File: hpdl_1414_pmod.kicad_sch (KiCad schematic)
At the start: 2 parts, among them J1 10129382-912001BLF, J2 10129382-912001BLF

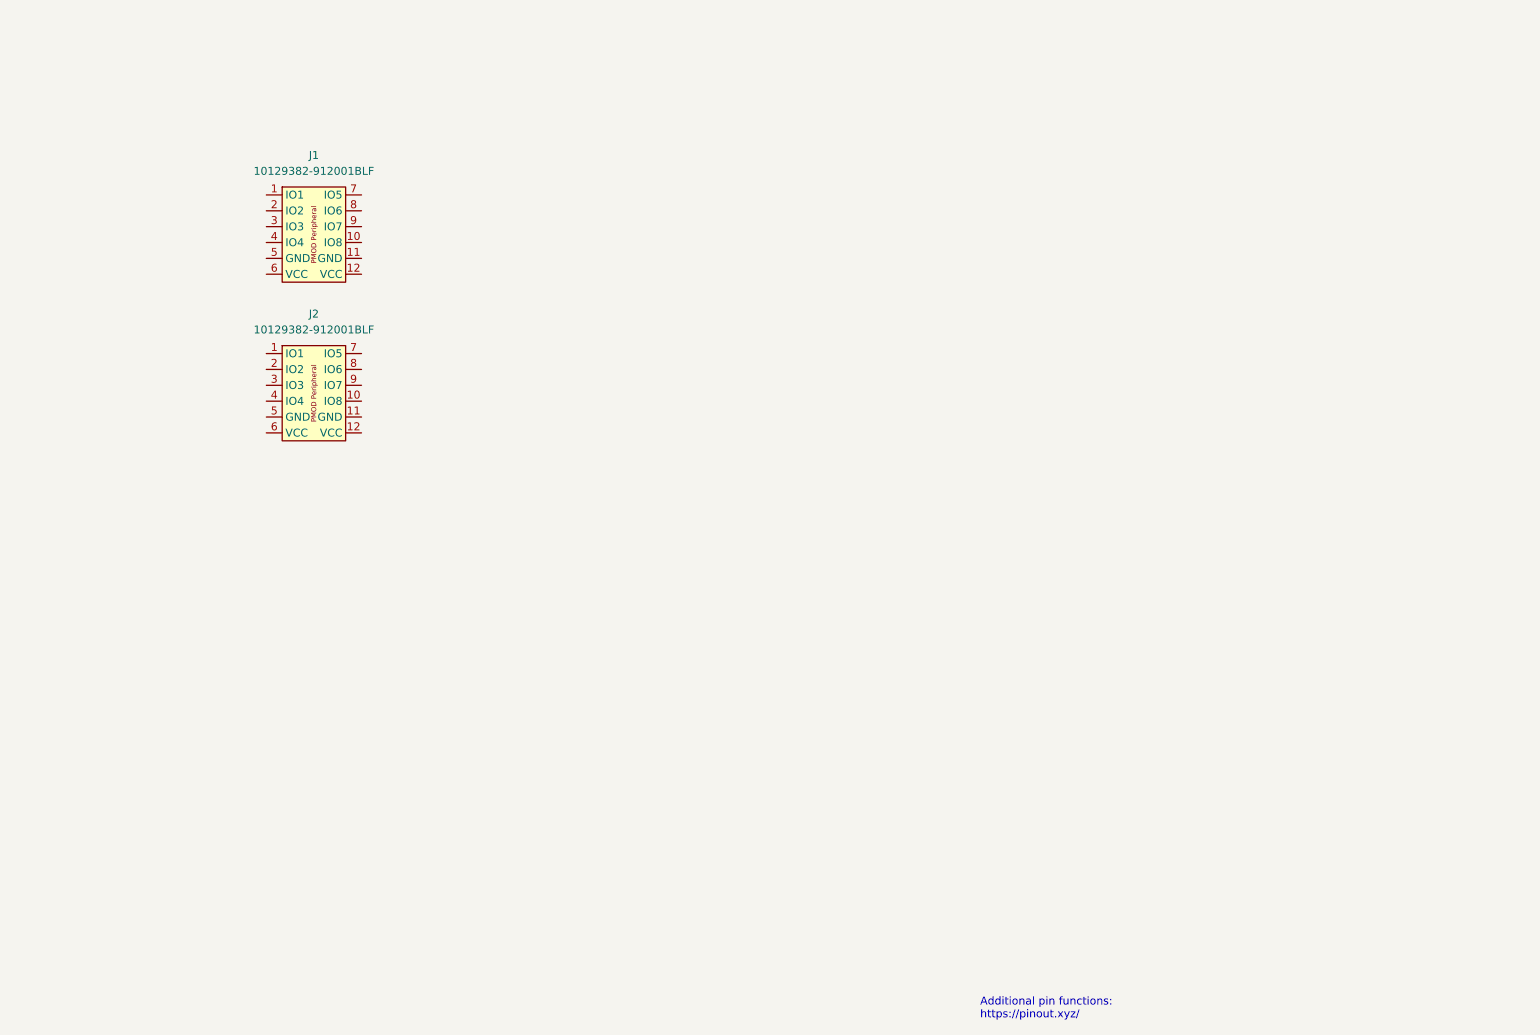
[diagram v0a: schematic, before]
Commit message: Finilize shematic, place components, add 3d models
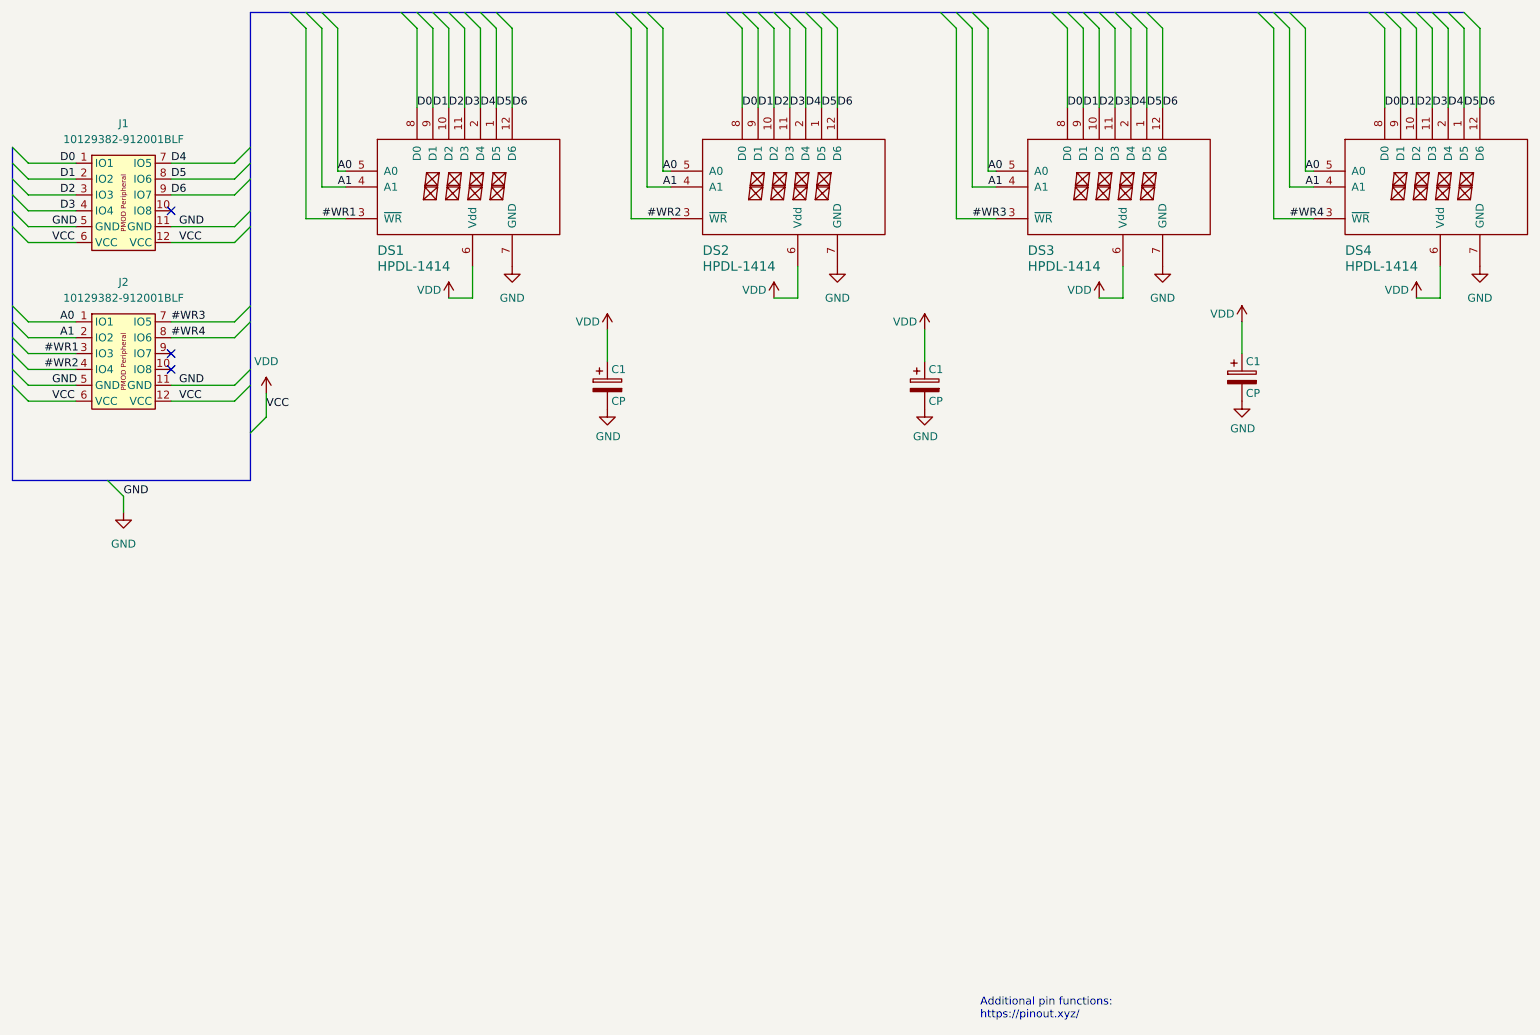
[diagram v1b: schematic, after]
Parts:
- added C1 (x3): CP, Capacitor_THT:C_Disc_D4.3mm_W1.9mm_P5.00mm, symbol Device:CP
- added DS1, DS2, DS3, DS4: HPDL-1414, hpdl_1414:hpdl-1414, symbol hpdl-1414:HPDL-1414
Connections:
- net A0: now reaches J2.1 (IO1)
- net A0: now also DS1.5 (A0), DS2.5 (A0), DS3.5 (A0), DS4.5 (A0)
- net GND: now reaches J2.11 (GND)
- net GND: now also J1.11 (GND), J1.5 (GND), J2.5 (GND), C1.2, C1.2, C1.2, DS1.7 (GND), DS2.7 (GND), DS3.7 (GND), DS4.7 (GND)
- net VDD: now reaches J2.12 (VCC)
- net VDD: now also J1.12 (VCC), J1.6 (VCC), J2.6 (VCC), C1.1, C1.1, C1.1, DS1.6 (Vdd), DS2.6 (Vdd), DS3.6 (Vdd), DS4.6 (Vdd)
- net A1: now reaches J2.2 (IO2)
- net A1: now also DS1.4 (A1), DS2.4 (A1), DS3.4 (A1), DS4.4 (A1)
- net #WR1: now reaches J2.3 (IO3)
- net #WR1: now also DS1.3 (~{WR})
- net #WR2: now reaches J2.4 (IO4)
- net #WR2: now also DS2.3 (~{WR})
- net #WR3: now reaches J2.7 (IO5)
- net #WR3: now also DS3.3 (~{WR})
- net #WR4: now reaches J2.8 (IO6)
- net #WR4: now also DS4.3 (~{WR})
- net D0: now reaches J1.1 (IO1)
- net D0: now also DS1.8 (D0), DS2.8 (D0), DS3.8 (D0), DS4.8 (D0)
- net D1: now reaches J1.2 (IO2)
- net D1: now also DS1.9 (D1), DS2.9 (D1), DS3.9 (D1), DS4.9 (D1)
- net D2: now reaches J1.3 (IO3)
- net D2: now also DS1.10 (D2), DS2.10 (D2), DS3.10 (D2), DS4.10 (D2)
- net D3: now reaches J1.4 (IO4)
- net D3: now also DS1.11 (D3), DS2.11 (D3), DS3.11 (D3), DS4.11 (D3)
- net D4: now reaches J1.7 (IO5)
- net D4: now also DS1.2 (D4), DS2.2 (D4), DS3.2 (D4), DS4.2 (D4)
- net D5: now reaches J1.8 (IO6)
- net D5: now also DS1.1 (D5), DS2.1 (D5), DS3.1 (D5), DS4.1 (D5)
- net D6: now reaches J1.9 (IO7)
- net D6: now also DS1.12 (D6), DS2.12 (D6), DS3.12 (D6), DS4.12 (D6)
- no-connect marks 0 -> 3
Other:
- moved on the sheet: J1, J2

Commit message: Grenerate gerbers, V1.0
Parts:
- added C7: 15uF, Capacitor_SMD:C_1210_3225Metric_Pad1.33x2.70mm_HandSolder, symbol Device:C_Small
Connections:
- net GND: now also C7.1
- net VDD: now also C7.2
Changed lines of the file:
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@@
+    (stroke (width 0) (type default))
+  )
+  (wire (pts (xy 80.01 78.74) (xy 80.01 81.28))
     (stroke (width 0) (type default))
   )
@@
   )
   (wire (pts (xy 93.98 21.59) (xy 93.98 34.29))
+    (stroke (width 0) (type default))
+  )
+  (wire (pts (xy 80.01 69.85) (xy 80.01 73.66))
     (stroke (width 0) (type default))
   )
@@
     )
   )
+  (symbol (lib_id "power:GND") (at 80.01 81.28 0) (unit 1)
+    (in_bom yes) (on_board yes) (dnp no)
+    (property "Reference" "#PWR033" (at 80.01 87.63 0)
+      (effects (font (size 1.27 1.27)) hide)
+    )
+    (property "Value" "GND" (at 80.137 85.6742 0)
+      (effects (font (size 1.27 1.27)))
+    )
+    (property "Footprint" "" (at 80.01 81.28 0)
+      (effects (font (size 1.27 1.27)) hide)
+    )
+    (property "Datasheet" "" (at 80.01 81.28 0)
+      (effects (font (size 1.27 1.27)) hide)
+    )
+    (pin "1")
+    (instances
+      (project "LTP305_ESP32_CLOCK"
+        (path "/c007e288-8439-49d9-bbdf-49724c34958c"
+          (reference "#PWR033") (unit 1)
+        )
+      )
+      (project "hpdl_1414_pmod"
+        (path "/e63e39d7-6ac0-4ffd-8aa3-1841a4541b55"
+          (reference "#PWR018") (unit 1)
+        )
+      )
+      (project "ltp_kikad"
+        (path "/eed35b77-cbf9-4596-9b17-2558f81058ba"
+          (reference "#PWR09") (unit 1)
+        )
+        (path "/eed35b77-cbf9-4596-9b17-2558f81058ba/eeffdcd2-f49f-4c6e-9443-50950813e7b1"
+          (reference "#PWR035") (unit 1)
+        )
+        (path "/eed35b77-cbf9-4596-9b17-2558f81058ba/7d22e16e-a0ba-4766-b1de-c8cbb28f14f7"
+          (reference "#PWR014") (unit 1)
+        )
+      )
+    )
+  )
   (symbol (lib_id "power:VDD") (at 93.98 64.77 0) (unit 1)
     (in_bom yes) (on_board yes) (dnp no)
@@
         (path "/e63e39d7-6ac0-4ffd-8aa3-1841a4541b55"
           (reference "#PWR03") (unit 1)
+        )
+      )
+    )
+  )
+  (symbol (lib_id "power:VDD") (at 80.01 69.85 0) (unit 1)
+    (in_bom yes) (on_board yes) (dnp no)
+    (property "Reference" "#PWR017" (at 80.01 73.66 0)
+      (effects (font (size 1.27 1.27)) hide)
+    )
+    (property "Value" "VDD" (at 74.93 68.58 0)
+      (effects (font (size 1.27 1.27)) (justify left))
+    )
+    (property "Footprint" "" (at 80.01 69.85 0)
+      (effects (font (size 1.27 1.27)) hide)
+    )
+    (property "Datasheet" "" (at 80.01 69.85 0)
+      (effects (font (size 1.27 1.27)) hide)
+    )
+    (pin "1")
+    (instances
+      (project "hpdl_1414_pmod"
+        (path "/e63e39d7-6ac0-4ffd-8aa3-1841a4541b55"
+          (reference "#PWR017") (unit 1)
         )
       )
@@
         )
       )
+    )
+  )
+  (symbol (lib_id "Device:C_Small") (at 80.01 76.2 180) (unit 1)
+    (in_bom yes) (on_board yes) (dnp no)
+    (property "Reference" "C7" (at 85.09 74.93 0)
+      (effects (font (size 1.27 1.27)))
+    )
+    (property "Value" "15uF" (at 85.09 77.47 0)
+      (effects (font (size 1.27 1.27)))
+    )
+    (property "Footprint" "Capacitor_SMD:C_1210_3225Metric_Pad1.33x2.70mm_HandSolder" (at 80.01 76.2 0)
+      (effects (font (size 1.27 1.27)) hide)
+    )
+    (property "Datasheet" "~" (at 80.01 76.2 0)
+      (effects (font (size 1.27 1.27)) hide)
+    )
+    (pin "1")
+    (pin "2")
+    (instances
+      (project "LTP305_ESP32_CLOCK"
+        (path "/c007e288-8439-49d9-bbdf-49724c34958c"
+          (reference "C7") (unit 1)
+        )
+      )
+      (project "hpdl_1414_pmod"
+        (path "/e63e39d7-6ac0-4ffd-8aa3-1841a4541b55"
+          (reference "C4") (unit 1)
+        )
+      )
+      (project "ltp_kikad"
+        (path "/eed35b77-cbf9-4596-9b17-2558f81058ba"
+          (reference "C6") (unit 1)
+        )
+        (path "/eed35b77-cbf9-4596-9b17-2558f81058ba/eeffdcd2-f49f-4c6e-9443-50950813e7b1"
+          (reference "C10") (unit 1)
+        )
+        (path "/eed35b77-cbf9-4596-9b17-2558f81058ba/7d22e16e-a0ba-4766-b1de-c8cbb28f14f7"
+          (reference "C2") (unit 1)
+        )
+      )
